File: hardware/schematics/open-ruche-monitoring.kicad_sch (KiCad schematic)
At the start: 0 parts

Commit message: hw(schematic): add sensors to schematic
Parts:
- added BZ1: Buzzer, symbol Device:Buzzer
- added J1: HX711, 110990030:SEEED_110990030, symbol Grove:110990030
- added J2: DHT22_EXT, 110990030:SEEED_110990030, symbol Grove:110990030
- added J3: DHT22_INT, 110990030:SEEED_110990030, symbol Grove:110990030
- added J4: SONDE_TEMP_1, 110990030:SEEED_110990030, symbol Grove:110990030
- added J5: SONDE_TEMP_2, 110990030:SEEED_110990030, symbol Grove:110990030
- added J6: Light Sensor, 110990030:SEEED_110990030, symbol Grove:110990030
- added J7: LORA, 110990030:SEEED_110990030, symbol Grove:110990030
- added R1: 4.7k, symbol Device:R_Small
- added R2: 100, symbol Device:R_Small
- added U1: uPesy_ESP32_Wroom_Low_Power_DevKit, uPesy Boards:uPesy_ESP32_Wroom_Low_Power_DevKit, symbol uPesy Boards:uPesy_ESP32_Wroom_Low_Power_DevKit
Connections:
- new net: BZ1.1 (+), R2.2
- new net +3.7V: J1.2 (VCC), J2.2 (VCC), J3.2 (VCC), J4.2 (VCC), J5.2 (VCC), J6.2 (VCC), J7.2 (VCC)
- new net +3.7v: R1.1
- new net BUZZER: R2.1, U1.22 (GPIO19)
- new net DATA_DHT22_EXT: J2.3 (SIG1), U1.10 (GPIO27)
- new net DATA_DHT22_INT: J3.3 (SIG1), U1.28 (GPIO0)
- new net DOUT: J1.3 (SIG1), U1.6 (GPIO32)
- new net GND: BZ1.2 (-), J1.1 (GND), J2.1 (GND), J3.1 (GND), J4.1 (GND), J5.1 (GND), J6.1 (GND), J7.1 (GND)
- new net ONE_WIRE_TEMP: J4.4 (SIG2), J5.4 (SIG2), R1.2, U1.27 (GPIO4)
- new net PSCK: J1.4 (SIG2), U1.7 (GPIO33)
- new net RX_LORA: J7.3 (SIG1), U1.25 (GPIO17)
- new net SCL: J6.3 (SIG1), U1.18 (GPIO22)
- new net SDA: J6.4 (SIG2), U1.21 (GPIO21)
- new net TX_LORA: J7.4 (SIG2), U1.26 (GPIO16)
- no-connect marks 0 -> 4
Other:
- title: (none) -> Open Ruche Monitoring

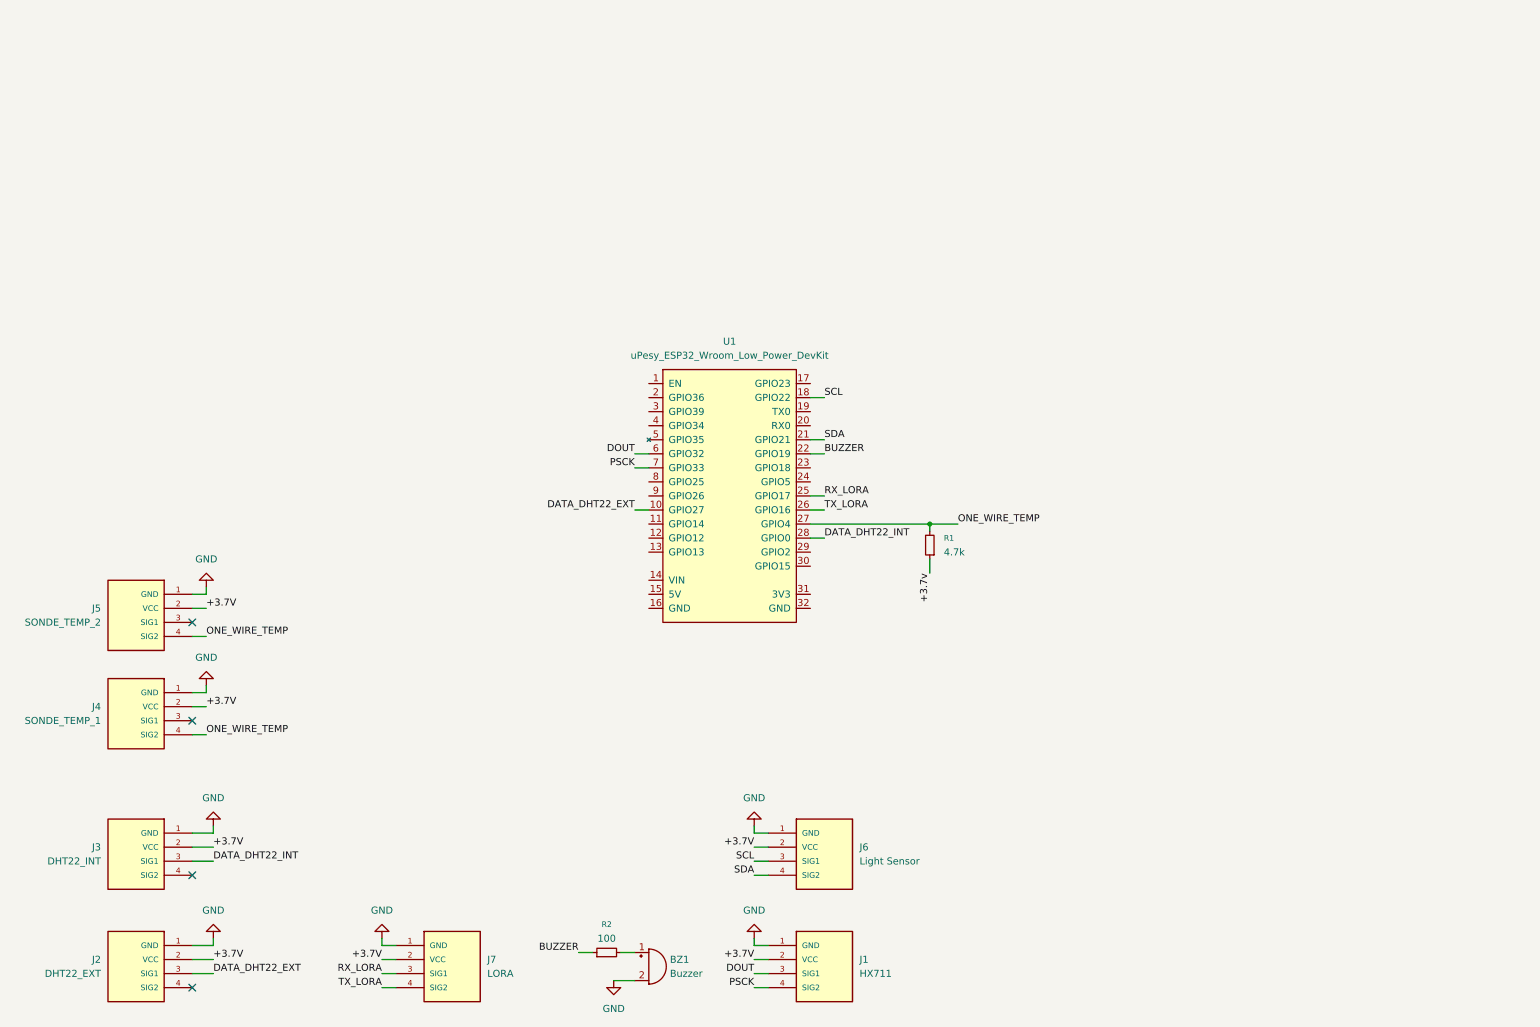
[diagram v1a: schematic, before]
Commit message: hw(schematic): add acc and 3.3V conversor schematic
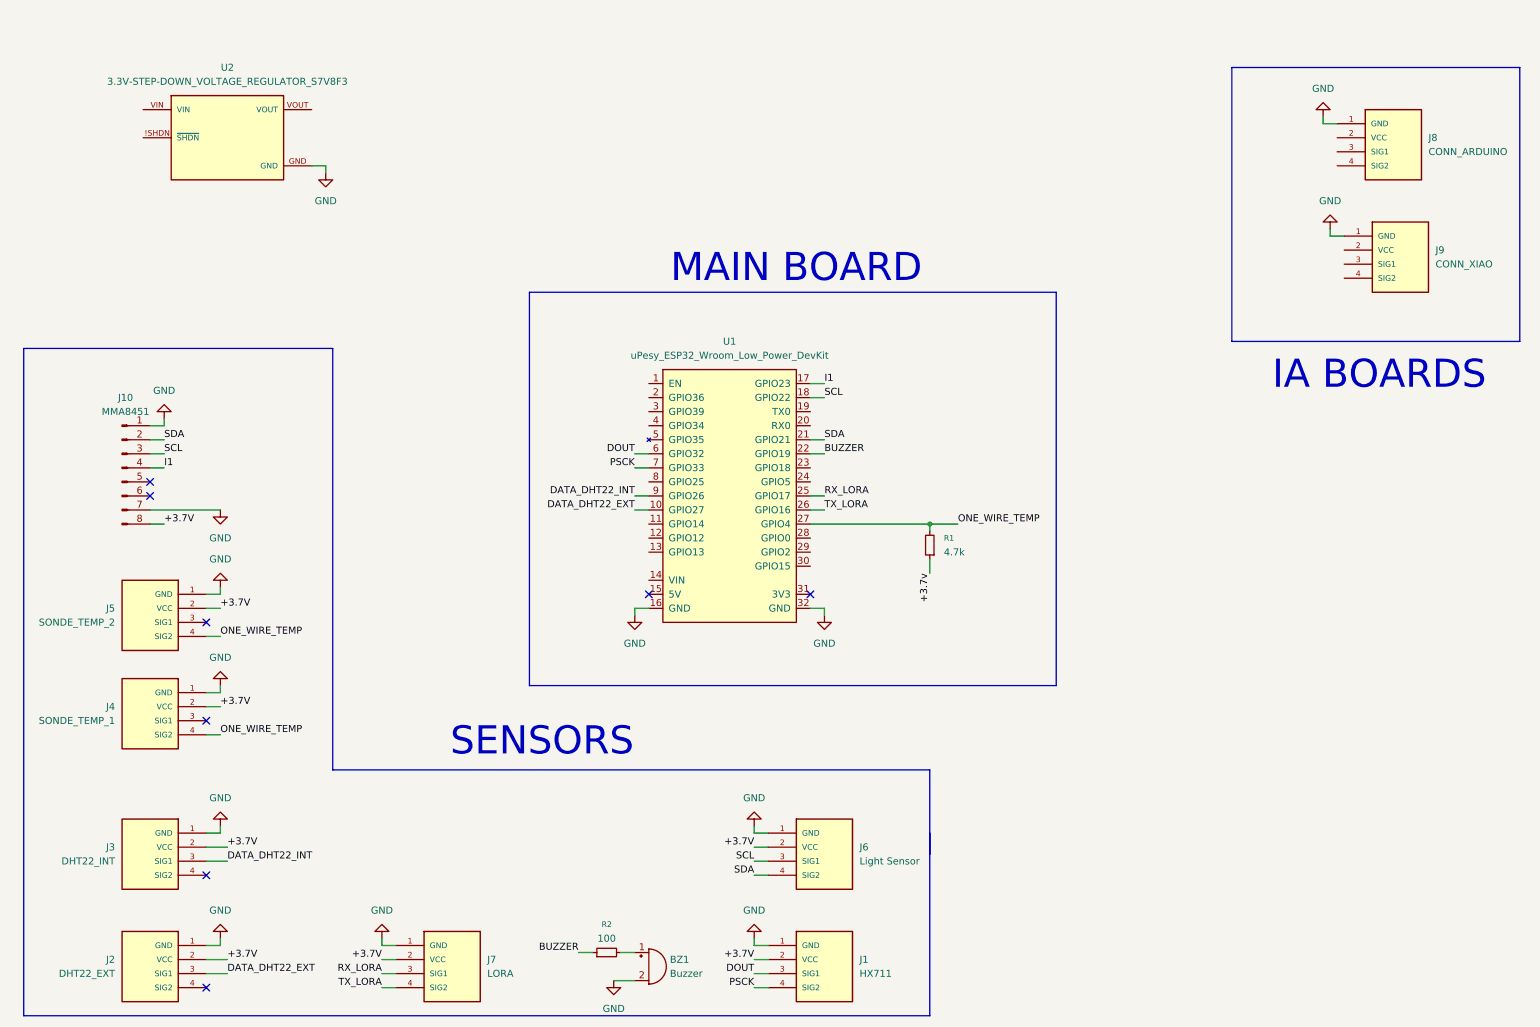
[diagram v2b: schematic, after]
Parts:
- added J10: MMA8451, Acc Adafruit:MODULE_2019, symbol Connector:Conn_01x08_Pin
- added J8: CONN_ARDUINO, 110990030:SEEED_110990030, symbol Grove:110990030
- added J9: CONN_XIAO, 110990030:SEEED_110990030, symbol Grove:110990030
- added U2: 3.3V-STEP-DOWN_VOLTAGE_REGULATOR_S7V8F3, Pololu:MODULE_STEP-DOWN_VOLTAGE_REGULATOR_D24V6F3, symbol Pololu:STEP-DOWN_VOLTAGE_REGULATOR_D24V6F3
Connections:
- net +3.7V: now also J10.8 (Pin_8)
- net DATA_DHT22_INT: now also U1.9 (GPIO26); no longer U1.28 (GPIO0)
- net GND: now also U1.16 (GND), U1.32 (GND), J10.1 (Pin_1), J10.7 (Pin_7), J8.1 (GND), J9.1 (GND), U2.GND
- net SCL: now also J10.3 (Pin_3)
- net SDA: now also J10.2 (Pin_2)
- net I1: now reaches U1.17 (GPIO23)
- net I1: now also J10.4 (Pin_4)
- no-connect marks 4 -> 8
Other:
- note added: "IA BOARDS"
- note added: "MAIN BOARD"
- note added: "SENSORS"
- moved on the sheet: J2, J3, J4, J5

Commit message: hw(schematic): schematic done
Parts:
- removed BZ1: Buzzer, symbol Device:Buzzer
- added C1, C3: 1u, Capacitor_SMD:C_0805_2012Metric, symbol Device:C_Small
- added C2, C4: 0.1u, Capacitor_SMD:C_0805_2012Metric, symbol Device:C_Small
- added J11: CONN_LIPO, Grove:SEEED_110990030, symbol Grove:110990030
- added J12: CONN_ALIM_ESP32, Connector_JST:JST_PH_B2B-PH-K_1x02_P2.00mm_Vertical, symbol Connector_Generic:Conn_01x02
- added LS1: KPEG222, KPEG222:KPEG222, symbol KPEG222:KPEG222
- added R3, R4: 1k, Resistor_SMD:R_0805_2012Metric, symbol Device:R_Small
- added R5, R6: 20k, Resistor_SMD:R_0805_2012Metric, symbol Device:R_Small
- added U3, U4: SiP32431DR3, Package_TO_SOT_SMD:SOT-363_SC-70-6, symbol Power_Management:SiP32431DR3
- J1, J2, J3, J4, J5, J6, J7, J8, J9: footprint 110990030:SEEED_110990030 -> Grove:SEEED_110990030
- R1, R2: footprint (none) -> Resistor_SMD:R_0805_2012Metric
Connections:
- net +3.7v is gone; now on net +3.7V: R1.1
- net +3.7V: now also U2.VIN, C1.2, C3.2, J11.2 (VCC), J12.1 (Pin_1), U3.4 (IN), U4.4 (IN); no longer J1.2 (VCC), J2.2 (VCC), J3.2 (VCC), J4.2 (VCC), J5.2 (VCC), J6.2 (VCC)
- net GND: now also C1.1, C2.2, C3.1, C4.2, J11.1 (GND), J12.2 (Pin_2), LS1.1 (-), R5.1, R6.1, U3.2 (GND), U3.5 (GND), U4.2 (GND), U4.5 (GND)
- net at R2.2: now also LS1.2 (+)
- net LS_XIAO_OUT: now reaches J9.2 (VCC)
- net LS_XIAO_OUT: now also C2.1, U3.1 (OUT)
- net at J9.3 (SIG1): now also R4.2
- net TX_ARDUINO: now reaches U1.11 (GPIO14)
- net TX_ARDUINO: now also R4.1
- net EN_SENSORS: now reaches U1.12 (GPIO12)
- net EN_SENSORS: now also R6.2, U4.3 (ON)
- net EN_ARDUINO: now reaches U1.13 (GPIO13)
- net EN_ARDUINO: now also U2.!SHDN (~{SHDN})
- net EN_XIAO: now reaches U1.23 (GPIO18)
- net EN_XIAO: now also R5.2, U3.3 (ON)
- net TX_XIAO: now reaches U1.8 (GPIO25)
- net TX_XIAO: now also R3.1
- net LS_ARDUINO_OUT: now reaches J8.2 (VCC)
- net LS_ARDUINO_OUT: now also U2.VOUT
- net at J8.3 (SIG1): now also R3.2
- new net LS_SENSORS_OUT: C4.1, J1.2 (VCC), J2.2 (VCC), J3.2 (VCC), J4.2 (VCC), J5.2 (VCC), J6.2 (VCC), U4.1 (OUT)
- no-connect marks 8 -> 10
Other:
- note added: "POWER"
- moved on the sheet: J7, J8, R2, U2

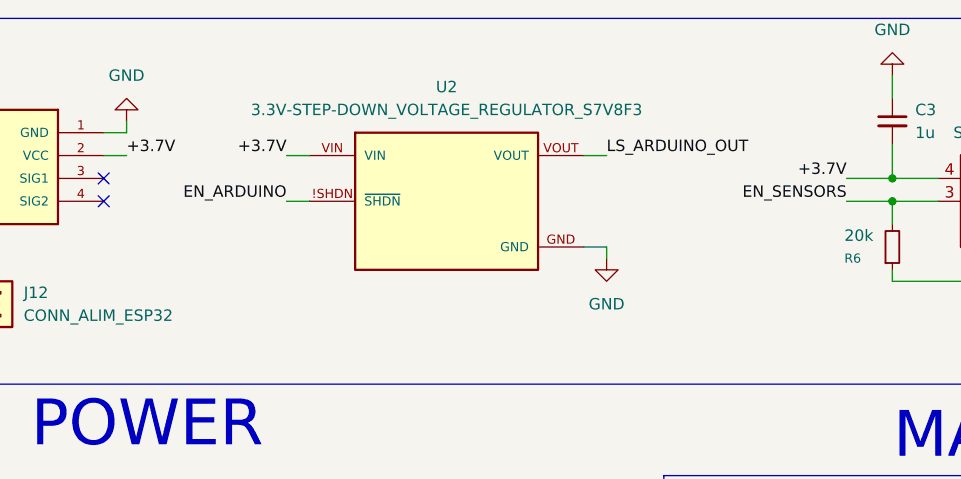
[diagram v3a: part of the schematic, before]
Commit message: hw(3D) Add 3D models for lora, hx711 and lipo charger
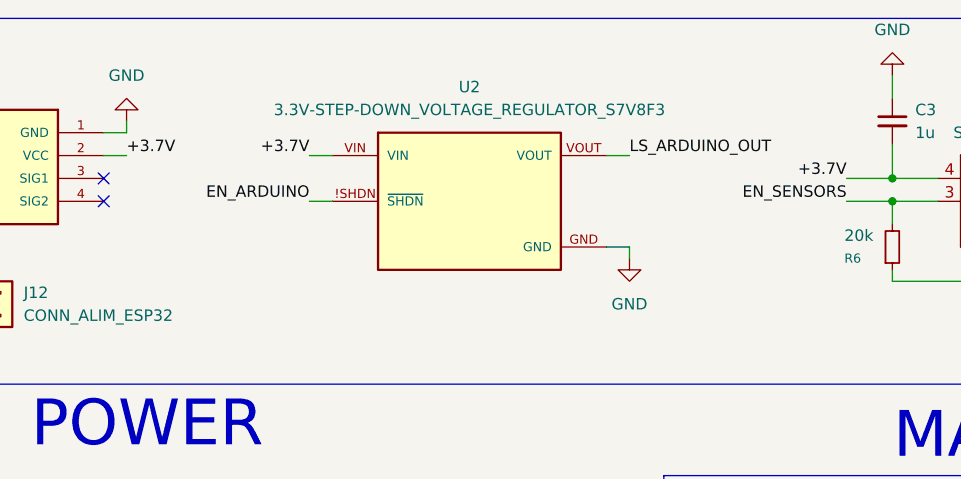
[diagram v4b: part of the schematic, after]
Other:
- moved on the sheet: U2
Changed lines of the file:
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@@
 	(wire
 		(pts
-			(xy 62.23 29.21) (xy 64.77 29.21)
+			(xy 64.77 29.21) (xy 67.31 29.21)
 		)
 		(stroke
@@
 	(wire
 		(pts
-			(xy 97.79 40.64) (xy 97.79 39.37)
+			(xy 100.33 40.64) (xy 100.33 39.37)
 		)
 		(stroke
@@
 	(wire
 		(pts
-			(xy 62.23 34.29) (xy 64.77 34.29)
+			(xy 64.77 34.29) (xy 67.31 34.29)
 		)
 		(stroke
@@
 	(wire
 		(pts
+			(xy 41.91 29.21) (xy 44.45 29.21)
+		)
+		(stroke
+			(width 0)
+			(type default)
+		)
+	)
+	(wire
+		(pts
 			(xy 125.73 121.92) (xy 123.19 121.92)
 		)
@@
 	(wire
 		(pts
-			(xy 95.25 29.21) (xy 97.79 29.21)
+			(xy 97.79 29.21) (xy 100.33 29.21)
 		)
 		(stroke
@@
 	(wire
 		(pts
-			(xy 95.25 39.37) (xy 97.79 39.37)
+			(xy 97.79 39.37) (xy 100.33 39.37)
 		)
 		(stroke
@@
 	(wire
 		(pts
-			(xy 41.91 29.21) (xy 44.45 29.21)
-		)
-		(stroke
-			(width 0)
-			(type default)
-		)
-	)
-	(wire
-		(pts
 			(xy 99.06 163.83) (xy 101.6 163.83)
 		)
@@
 	)
 	(label "+3.7V"
-		(at 62.23 29.21 180)
+		(at 64.77 29.21 180)
 		(effects
 			(font
@@
 	)
 	(label "LS_ARDUINO_OUT"
-		(at 97.79 29.21 0)
+		(at 100.33 29.21 0)
 		(effects
 			(font
@@
 	)
 	(label "EN_ARDUINO"
-		(at 62.23 34.29 180)
+		(at 64.77 34.29 180)
 		(effects
 			(font
@@
 	(symbol
 		(lib_id "power:GND")
-		(at 97.79 40.64 0)
+		(at 100.33 40.64 0)
 		(unit 1)
 		(exclude_from_sim no)
@@
 		(fields_autoplaced yes)
 		(property "Reference" "#PWR015"
-			(at 97.79 46.99 0)
+			(at 100.33 46.99 0)
 			(effects
 				(font
@@
 		)
 		(property "Value" "GND"
-			(at 97.79 45.72 0)
+			(at 100.33 45.72 0)
 			(effects
 				(font
@@
 		)
 		(property "Footprint" ""
-			(at 97.79 40.64 0)
+			(at 100.33 40.64 0)
 			(effects
 				(font
@@
 		)
 		(property "Datasheet" ""
-			(at 97.79 40.64 0)
+			(at 100.33 40.64 0)
 			(effects
 				(font
@@
 		)
 		(property "Description" "Power symbol creates a global label with name \"GND\" , ground"
-			(at 97.79 40.64 0)
+			(at 100.33 40.64 0)
 			(effects
 				(font
@@
 	(symbol
 		(lib_id "Pololu:STEP-DOWN_VOLTAGE_REGULATOR_D24V6F3")
-		(at 80.01 34.29 0)
+		(at 82.55 34.29 0)
 		(unit 1)
 		(exclude_from_sim no)
@@
 		(fields_autoplaced yes)
 		(property "Reference" "U2"
-			(at 80.01 21.59 0)
+			(at 82.55 21.59 0)
 			(effects
 				(font
@@
 		)
 		(property "Value" "3.3V-STEP-DOWN_VOLTAGE_REGULATOR_S7V8F3"
-			(at 80.01 24.13 0)
+			(at 82.55 24.13 0)
 			(effects
 				(font
@@
 		)
 		(property "Footprint" "Pololu:MODULE_STEP-DOWN_VOLTAGE_REGULATOR_D24V6F3"
-			(at 80.01 34.29 0)
+			(at 82.55 34.29 0)
 			(effects
 				(font
@@
 		)
 		(property "Datasheet" ""
-			(at 80.01 34.29 0)
+			(at 82.55 34.29 0)
 			(effects
 				(font
@@
 		)
 		(property "Description" ""
-			(at 80.01 34.29 0)
+			(at 82.55 34.29 0)
 			(effects
 				(font
@@
 		)
 		(property "MF" "Pololu"
-			(at 80.01 34.29 0)
+			(at 82.55 34.29 0)
 			(effects
 				(font
@@
 		)
 		(property "MAXIMUM_PACKAGE_HEIGHT" "2.54mm"
-			(at 80.01 34.29 0)
+			(at 82.55 34.29 0)
 			(effects
 				(font
@@
 		)
 		(property "CREATOR" "NEZY"
-			(at 80.01 34.29 0)
+			(at 82.55 34.29 0)
 			(effects
 				(font
@@
 		)
 		(property "Price" "None"
-			(at 80.01 34.29 0)
+			(at 82.55 34.29 0)
 			(effects
 				(font
@@
 		)
 		(property "Package" "None"
-			(at 80.01 34.29 0)
+			(at 82.55 34.29 0)
 			(effects
 				(font
@@
 		)
 		(property "Check_prices" "https://www.snapeda.com/parts/STEP-DOWN%20VOLTAGE%20REGULATOR%20D24V6F3/Pololu/view-part/?ref=eda"
-			(at 80.01 34.29 0)
+			(at 82.55 34.29 0)
 			(effects
 				(font
@@
 		)
 		(property "STANDARD" "Manufacturer Recommendations"
-			(at 80.01 34.29 0)
+			(at 82.55 34.29 0)
 			(effects
 				(font
@@
 		)
 		(property "PARTREV" "NA"
-			(at 80.01 34.29 0)
+			(at 82.55 34.29 0)
 			(effects
 				(font
@@
 		)
 		(property "VERIFIER" ""
-			(at 80.01 34.29 0)
+			(at 82.55 34.29 0)
 			(effects
 				(font
@@
 		)
 		(property "SnapEDA_Link" "https://www.snapeda.com/parts/STEP-DOWN%20VOLTAGE%20REGULATOR%20D24V6F3/Pololu/view-part/?ref=snap"
-			(at 80.01 34.29 0)
+			(at 82.55 34.29 0)
 			(effects
 				(font
@@
 		)
 		(property "MP" "STEP-DOWN VOLTAGE REGULATOR D24V6F3"
-			(at 80.01 34.29 0)
+			(at 82.55 34.29 0)
 			(effects
 				(font
@@
 		)
 		(property "Description_1" "Converter: step down; Uin: 3.8÷42V; Uout: 3.3V; 600mA; 80÷90%"
-			(at 80.01 34.29 0)
+			(at 82.55 34.29 0)
 			(effects
 				(font
@@
 		)
 		(property "Availability" "Not in stock"
-			(at 80.01 34.29 0)
+			(at 82.55 34.29 0)
 			(effects
 				(font
@@
 		)
 		(property "MANUFACTURER" "Pololu"
-			(at 80.01 34.29 0)
+			(at 82.55 34.29 0)
 			(effects
 				(font

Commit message: hw(pcb) save pcb to try another layout
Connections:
- net EN_SENSORS: now also U1.23 (GPIO18); no longer U1.12 (GPIO12)
- net EN_XIAO: now also U1.12 (GPIO12); no longer U1.23 (GPIO18)
- no-connect marks 10 -> 24
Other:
- moved on the sheet: R6

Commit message: hw(pcb) pcb done
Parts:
- removed C1, C3: 1u, Capacitor_SMD:C_0805_2012Metric, symbol Device:C_Small
- removed C2, C4: 0.1u, Capacitor_SMD:C_0805_2012Metric, symbol Device:C_Small
- removed R5, R6: 20k, Resistor_SMD:R_0805_2012Metric, symbol Device:R_Small
- removed U3, U4: SiP32431DR3, Package_TO_SOT_SMD:SOT-363_SC-70-6, symbol Power_Management:SiP32431DR3
- added U3: S7V8F5, Pololu:MODULE_STEP-DOWN_VOLTAGE_REGULATOR_D24V6F3, symbol Pololu:STEP-DOWN_VOLTAGE_REGULATOR_D24V6F3
- R1, R2, R3, R4: footprint Resistor_SMD:R_0805_2012Metric -> Resistor_THT:R_Axial_DIN0207_L6.3mm_D2.5mm_P10.16mm_Horizontal
- U2: value 3.3V-STEP-DOWN_VOLTAGE_REGULATOR_S7V8F3 -> S7V8F3
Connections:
- net EN_XIAO is gone; now on net EN_3.3V_REG: U1.12 (GPIO12)
- net LS_SENSORS_OUT is gone; now on net +3.3V_REG: J1.2 (VCC), J2.2 (VCC), J3.2 (VCC), J4.2 (VCC), J5.2 (VCC), J6.2 (VCC)
- net +3.7V: now also U3.VIN; no longer J10.8 (Pin_8), J7.2 (VCC), R1.1
- net GND: now also U3.GND; no longer J10.1 (Pin_1)
- net TX_ARDUINO: now also R3.1; no longer R4.1
- net TX_XIAO: now also R4.1; no longer R3.1
- net +3.3V: now reaches U1.31 (3V3)
- net +3.3V: now also J10.8 (Pin_8), R1.1
- net EN_ARDUINO renamed EN_3.3V_REG
- net EN_3.3V_REG: no longer U1.13 (GPIO13)
- net EN_SENSORS: no longer names the net of U1.23 (GPIO18)
- net LS_ARDUINO_OUT renamed +3.3V_REG
- net +3.3V_REG: now also J7.2 (VCC); no longer J8.2 (VCC)
- net LS_XIAO_OUT renamed +5V_REG
- net +5V_REG: now also J8.2 (VCC), U3.VOUT
- new net EN_5V_REG: U1.13 (GPIO13), U3.!SHDN (~{SHDN})
- no-connect marks 24 -> 25
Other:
- moved on the sheet: U2
